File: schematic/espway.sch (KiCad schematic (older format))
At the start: 32 parts, among them J1 CONN_01X02, J2 CONN_01X02, J3 CONN_01X04_MALE, SW1 SW_Push, U1 LM1117-3.3, U2 ESP-12E, U3 DRV8835, U4 LSM6DS3

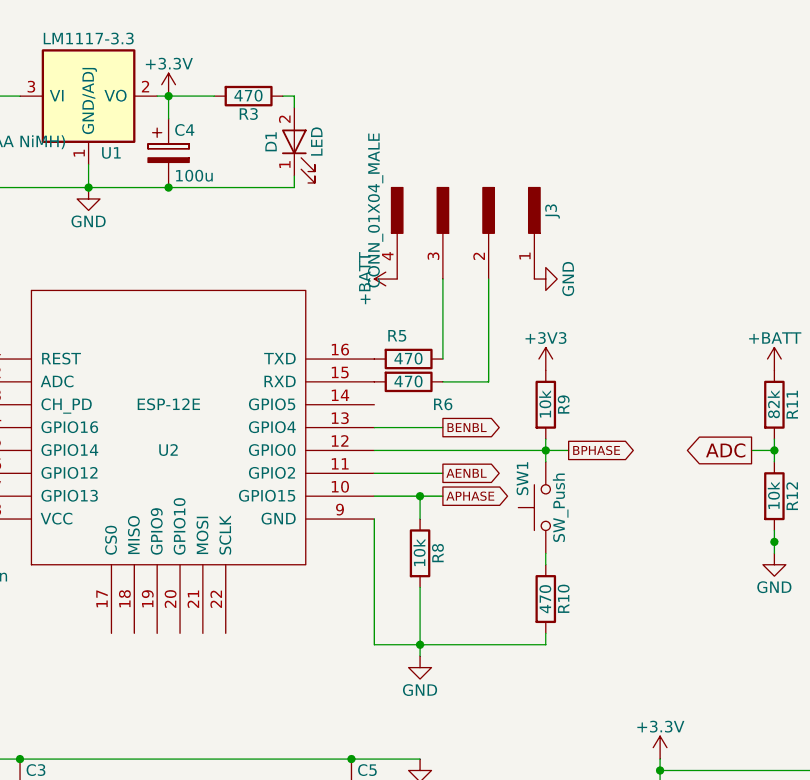
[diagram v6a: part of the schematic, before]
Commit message: Schematic: change resistor values, break out extra GPIO pin
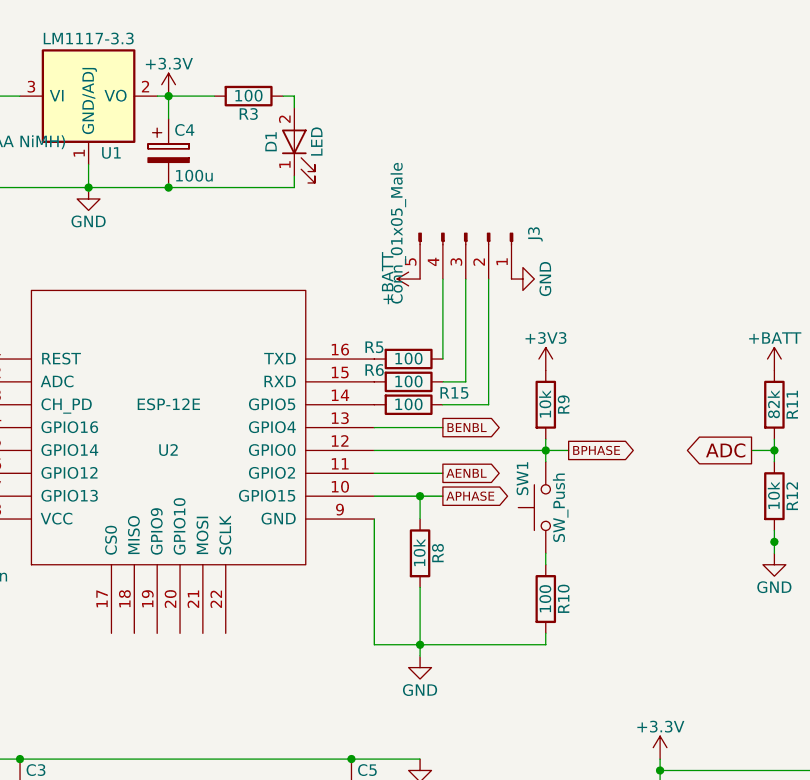
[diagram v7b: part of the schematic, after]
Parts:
- removed J3: CONN_01X04_MALE, Pin_Headers:Pin_Header_Angled_1x04_Pitch2.54mm, symbol CONN_01X04_MALE
- added J3: Conn_01x05_Male, Pin_Headers:Pin_Header_Angled_1x05_Pitch2.54mm, symbol Conn_01x05_Male
- added R15: 100, Resistors_SMD:R_0603, symbol R
- R10, R3, R5, R6: value 470 -> 100
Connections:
- net +BATT: now also J3.5 (Pin_5)
- net GND: now also J3.1 (Pin_1)
- net at U2.14 (GPIO5): now also R15.2
- net at R5.1: now also J3.4 (Pin_4)
- net at R6.1: now also J3.3 (Pin_3)
- new net: J3.2 (Pin_2), R15.1
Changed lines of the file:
@@
 U 1 1 59B6D1FB
 P 7250 2350
-F 0 "R5" V 7150 2300 50  0000 C CNN
-F 1 "470" V 7250 2350 50  0000 C CNN
+F 0 "R5" V 7200 2200 50  0000 C CNN
+F 1 "100" V 7250 2350 50  0000 C CNN
 F 2 "Resistors_SMD:R_0603" V 7180 2350 50  0001 C CNN
 F 3 "" H 7250 2350 50  0001 C CNN
@@
 U 1 1 59B6D22A
 P 7250 2450
-F 0 "R6" V 7350 2600 50  0000 C CNN
-F 1 "470" V 7250 2450 50  0000 C CNN
+F 0 "R6" V 7200 2300 50  0000 C CNN
+F 1 "100" V 7250 2450 50  0000 C CNN
 F 2 "Resistors_SMD:R_0603" V 7180 2450 50  0001 C CNN
 F 3 "" H 7250 2450 50  0001 C CNN
@@
 L GND #PWR05
 U 1 1 59B8139A
-P 7800 2000
-F 0 "#PWR05" H 7800 1750 50  0001 C CNN
-F 1 "GND" H 7800 1850 50  0000 C CNN
-F 2 "" H 7800 2000 50  0001 C CNN
-F 3 "" H 7800 2000 50  0001 C CNN
-	1    7800 2000
+P 7700 2000
+F 0 "#PWR05" H 7700 1750 50  0001 C CNN
+F 1 "GND" H 7700 1850 50  0000 C CNN
+F 2 "" H 7700 2000 50  0001 C CNN
+F 3 "" H 7700 2000 50  0001 C CNN
+	1    7700 2000
 	0    -1   -1   0
 $EndComp
@@
 P 7850 3400
 F 0 "R10" V 7930 3400 50  0000 C CNN
-F 1 "470" V 7850 3400 50  0000 C CNN
+F 1 "100" V 7850 3400 50  0000 C CNN
 F 2 "Resistors_SMD:R_0603" V 7780 3400 50  0001 C CNN
 F 3 "" H 7850 3400 50  0001 C CNN
@@
 $EndComp
 $Comp
-L CONN_01X04_MALE J3
-U 1 1 59B95DFA
-P 7500 1700
-F 0 "J3" H 7500 2075 50  0000 C CNN
-F 1 "CONN_01X04_MALE" H 7500 1300 50  0000 C CNN
-F 2 "Pin_Headers:Pin_Header_Angled_1x04_Pitch2.54mm" H 7500 2000 50  0001 C CNN
-F 3 "" H 7500 2000 50  0001 C CNN
-	1    7500 1700
-	0    1    1    0
-$EndComp
-$Comp
 L DRV8835 U3
 U 1 1 59BA4BA8
@@
 P 6550 1200
 F 0 "R3" V 6630 1200 50  0000 C CNN
-F 1 "470" V 6550 1200 50  0000 C CNN
+F 1 "100" V 6550 1200 50  0000 C CNN
 F 2 "Resistors_SMD:R_0603" V 6480 1200 50  0001 C CNN
 F 3 "" H 6550 1200 50  0001 C CNN
@@
 Connection ~ 7300 3600
 Wire Wire Line
-	7400 2450 7600 2450
-Wire Wire Line
-	7600 2450 7600 2000
-Wire Wire Line
 	7400 2350 7400 2000
 Wire Wire Line
@@
 L +BATT #PWR019
 U 1 1 5A1E0D39
-P 7200 2000
-F 0 "#PWR019" H 7200 1850 50  0001 C CNN
-F 1 "+BATT" H 7200 2140 50  0000 C CNN
-F 2 "" H 7200 2000 50  0001 C CNN
-F 3 "" H 7200 2000 50  0001 C CNN
-	1    7200 2000
+P 7300 2000
+F 0 "#PWR019" H 7300 1850 50  0001 C CNN
+F 1 "+BATT" H 7300 2140 50  0000 C CNN
+F 2 "" H 7300 2000 50  0001 C CNN
+F 3 "" H 7300 2000 50  0001 C CNN
+	1    7300 2000
 	0    -1   -1   0
 $EndComp
+$Comp
+L Conn_01x05_Male J3
+U 1 1 5A42CC5F
+P 7500 1800
+F 0 "J3" H 7500 2100 50  0000 C CNN
+F 1 "Conn_01x05_Male" H 7500 1500 50  0000 C CNN
+F 2 "Pin_Headers:Pin_Header_Angled_1x05_Pitch2.54mm" H 7500 1800 50  0001 C CNN
+F 3 "" H 7500 1800 50  0001 C CNN
+	1    7500 1800
+	0    1    1    0
+$EndComp
+$Comp
+L R R15
+U 1 1 5A42CEC2
+P 7250 2550
+F 0 "R15" V 7200 2750 50  0000 C CNN
+F 1 "100" V 7250 2550 50  0000 C CNN
+F 2 "Resistors_SMD:R_0603" V 7180 2550 50  0001 C CNN
+F 3 "" H 7250 2550 50  0001 C CNN
+	1    7250 2550
+	0    1    1    0
+$EndComp
+Wire Wire Line
+	7400 2450 7500 2450
+Wire Wire Line
+	7500 2450 7500 2000
+Wire Wire Line
+	7400 2550 7600 2550
+Wire Wire Line
+	7600 2550 7600 2000
 $EndSCHEMATC

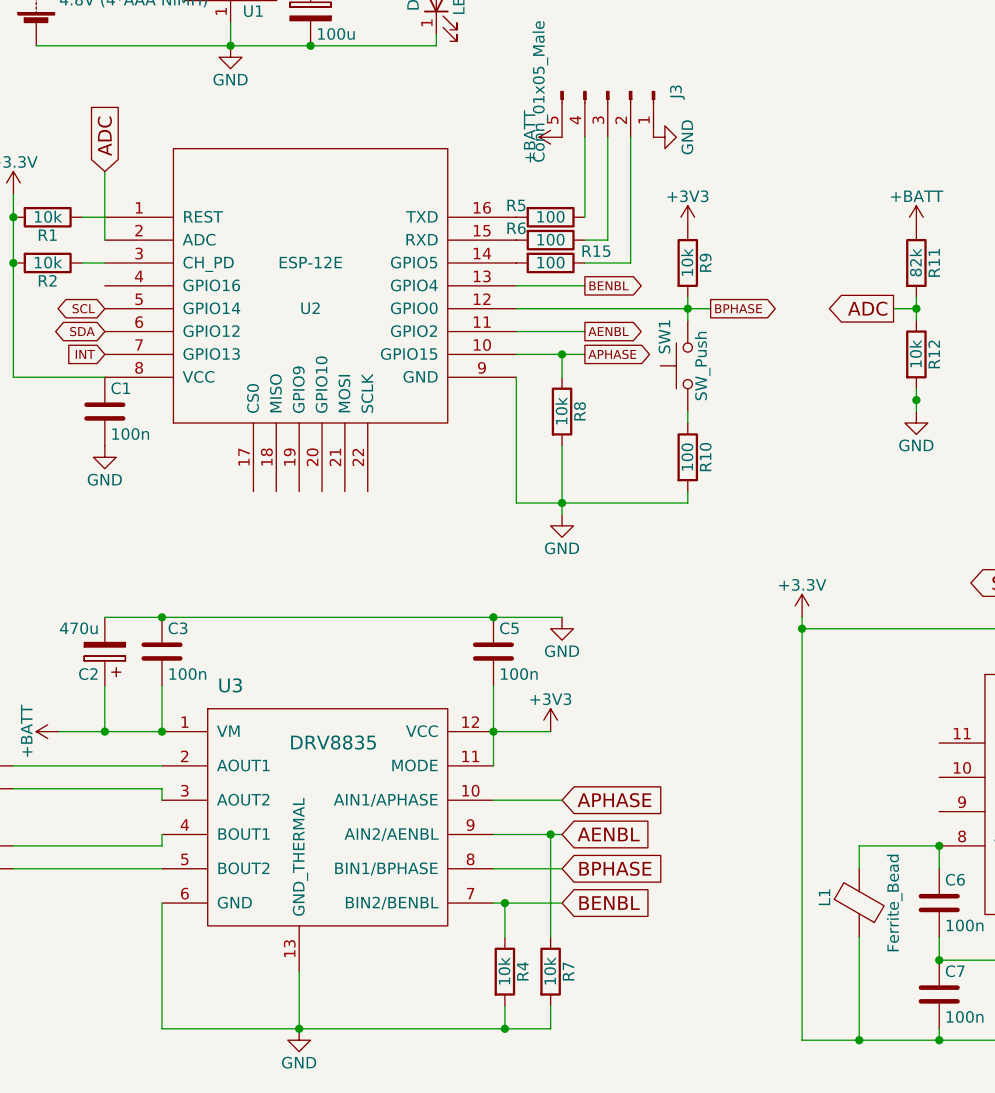
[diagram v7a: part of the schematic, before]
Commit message: schematic & pcb: pullup fixes etc
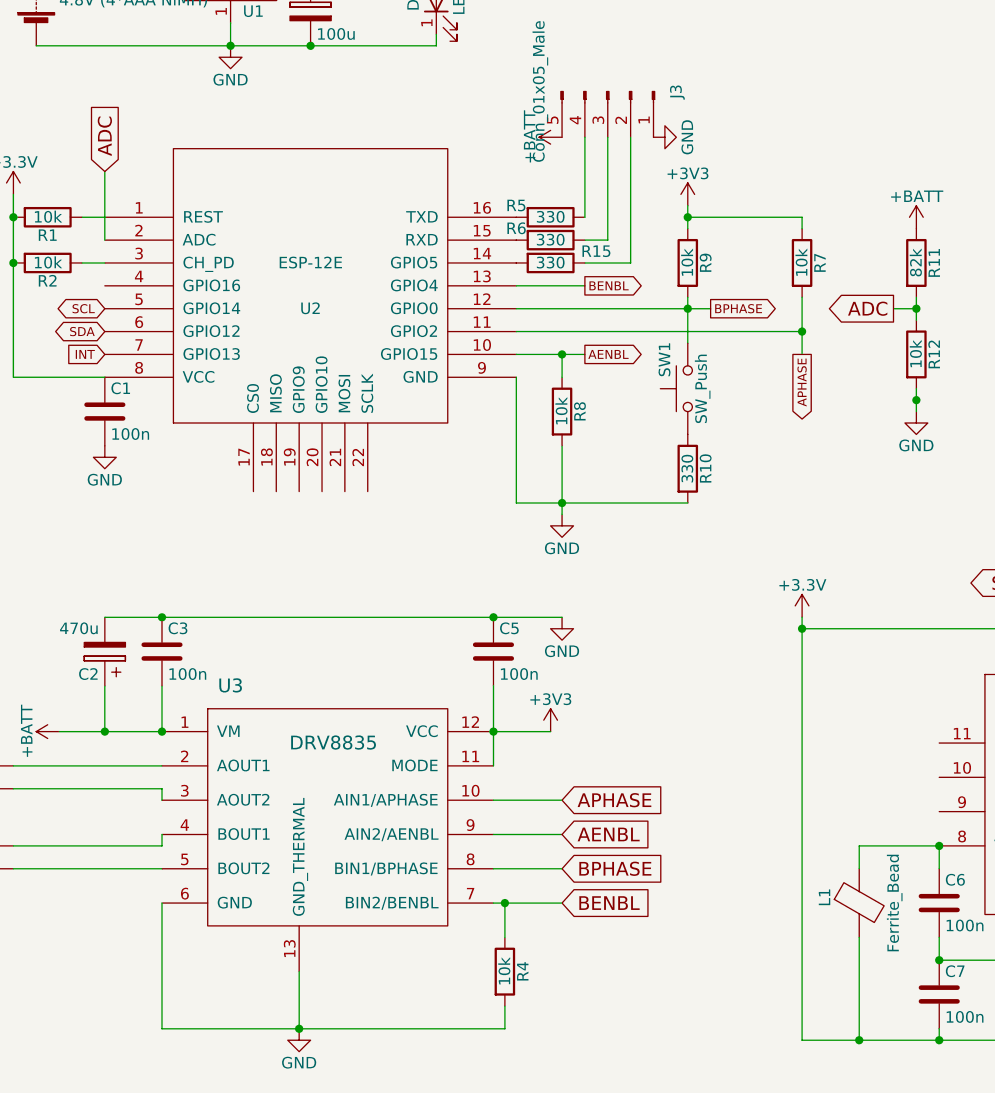
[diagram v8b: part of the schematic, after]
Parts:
- R10, R15, R5, R6: value 100 -> 330
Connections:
- net +3V3: now also R7.1
- net AENBL: now also R8.1, U2.10 (GPIO15); no longer R7.1, U2.11 (GPIO2)
- net APHASE: now also R7.2, U2.11 (GPIO2); no longer R8.1, U2.10 (GPIO15)
- net GND: no longer R7.2
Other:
- moved on the sheet: R10, SW1
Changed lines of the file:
@@
 P 7250 2350
 F 0 "R5" V 7200 2200 50  0000 C CNN
-F 1 "100" V 7250 2350 50  0000 C CNN
+F 1 "330" V 7250 2350 50  0000 C CNN
 F 2 "Resistors_SMD:R_0603" V 7180 2350 50  0001 C CNN
 F 3 "" H 7250 2350 50  0001 C CNN
@@
 P 7250 2450
 F 0 "R6" V 7200 2300 50  0000 C CNN
-F 1 "100" V 7250 2450 50  0000 C CNN
+F 1 "330" V 7250 2450 50  0000 C CNN
 F 2 "Resistors_SMD:R_0603" V 7180 2450 50  0001 C CNN
 F 3 "" H 7250 2450 50  0001 C CNN
@@
 L R R10
 U 1 1 59B81CF0
-P 7850 3400
-F 0 "R10" V 7930 3400 50  0000 C CNN
-F 1 "100" V 7850 3400 50  0000 C CNN
-F 2 "Resistors_SMD:R_0603" V 7780 3400 50  0001 C CNN
-F 3 "" H 7850 3400 50  0001 C CNN
-	1    7850 3400
+P 7850 3450
+F 0 "R10" V 7930 3450 50  0000 C CNN
+F 1 "330" V 7850 3450 50  0000 C CNN
+F 2 "Resistors_SMD:R_0603" V 7780 3450 50  0001 C CNN
+F 3 "" H 7850 3450 50  0001 C CNN
+	1    7850 3450
 	1    0    0    -1
 $EndComp
@@
 L SW_Push SW1
 U 1 1 59B81E53
-P 7850 3000
-F 0 "SW1" H 7900 3100 50  0000 L CNN
-F 1 "SW_Push" H 7850 2940 50  0000 C CNN
-F 2 "Buttons_Switches_SMD:SW_SPST_KMR2" H 7850 3200 50  0001 C CNN
-F 3 "" H 7850 3200 50  0001 C CNN
-	1    7850 3000
+P 7850 3100
+F 0 "SW1" H 7900 3200 50  0000 L CNN
+F 1 "SW_Push" H 7850 3040 50  0000 C CNN
+F 2 "Buttons_Switches_SMD:SW_SPST_KMR2" H 7850 3300 50  0001 C CNN
+F 3 "" H 7850 3300 50  0001 C CNN
+	1    7850 3100
 	0    -1   -1   0
 $EndComp
@@
 BENBL
 Text GLabel 7400 2950 2    39   Output ~ 0
-APHASE
+AENBL
 $Comp
 L Battery BT1
@@
 Connection ~ 6200 1600
 $Comp
-L R R7
-U 1 1 59E13532
-P 7250 5650
-F 0 "R7" V 7330 5650 50  0000 C CNN
-F 1 "10k" V 7250 5650 50  0000 C CNN
-F 2 "Resistors_SMD:R_0603" V 7180 5650 50  0001 C CNN
-F 3 "" H 7250 5650 50  0001 C CNN
-	1    7250 5650
-	1    0    0    -1
-$EndComp
-$Comp
 L GND #PWR015
 U 1 1 5A19A5EC
@@
 Wire Wire Line
 	5550 5350 5550 5900
-Wire Wire Line
-	5550 5900 7250 5900
 Connection ~ 6150 5900
 Wire Wire Line
@@
 Wire Wire Line
 	7050 5900 7050 5800
-Connection ~ 7050 5900
 Wire Wire Line
 	7100 2950 7400 2950
@@
 Wire Wire Line
 	7100 3050 7100 3600
-Text GLabel 7400 2850 2    39   Output ~ 0
-AENBL
-Wire Wire Line
-	7400 2850 7100 2850
+Text GLabel 8350 2950 3    39   Output ~ 0
+APHASE
+Wire Wire Line
+	7100 2850 8350 2850
 Text GLabel 7400 2650 2    39   Output ~ 0
 BENBL
@@
 	7000 5050 7300 5050
 Wire Wire Line
-	7250 5050 7250 5500
-Connection ~ 7250 5050
-Wire Wire Line
-	7250 5900 7250 5800
-Wire Wire Line
 	7300 5200 7000 5200
 Wire Wire Line
@@
 Wire Wire Line
 	10200 4650 10050 4650
-Wire Wire Line
-	7850 3600 7850 3550
 Connection ~ 8850 3150
-Wire Wire Line
-	7850 3250 7850 3200
 $Comp
 L R R9
@@
 L +3V3 #PWR018
 U 1 1 5A1DE58F
-P 7850 2400
-F 0 "#PWR018" H 7850 2250 50  0001 C CNN
-F 1 "+3V3" H 7850 2540 50  0000 C CNN
-F 2 "" H 7850 2400 50  0001 C CNN
-F 3 "" H 7850 2400 50  0001 C CNN
-	1    7850 2400
-	1    0    0    -1
-$EndComp
-Wire Wire Line
-	7850 2700 7850 2800
+P 7850 2300
+F 0 "#PWR018" H 7850 2150 50  0001 C CNN
+F 1 "+3V3" H 7850 2440 50  0000 C CNN
+F 2 "" H 7850 2300 50  0001 C CNN
+F 3 "" H 7850 2300 50  0001 C CNN
+	1    7850 2300
+	1    0    0    -1
+$EndComp
+Wire Wire Line
+	7850 2700 7850 2900
 Text GLabel 7950 2750 2    39   Output ~ 0
 BPHASE
@@
 P 7250 2550
 F 0 "R15" V 7200 2750 50  0000 C CNN
-F 1 "100" V 7250 2550 50  0000 C CNN
+F 1 "330" V 7250 2550 50  0000 C CNN
 F 2 "Resistors_SMD:R_0603" V 7180 2550 50  0001 C CNN
 F 3 "" H 7250 2550 50  0001 C CNN
@@
 Wire Wire Line
 	7600 2550 7600 2000
+Wire Wire Line
+	5550 5900 7050 5900
+Wire Wire Line
+	7850 2300 7850 2400
+$Comp
+L R R7
+U 1 1 5A442EE2
+P 8350 2550
+F 0 "R7" V 8430 2550 50  0000 C CNN
+F 1 "10k" V 8350 2550 50  0000 C CNN
+F 2 "Resistors_SMD:R_0603" V 8280 2550 50  0001 C CNN
+F 3 "" H 8350 2550 50  0001 C CNN
+	1    8350 2550
+	1    0    0    -1
+$EndComp
+Wire Wire Line
+	8350 2700 8350 2950
+Wire Wire Line
+	8350 2400 8350 2350
+Wire Wire Line
+	8350 2350 7850 2350
+Connection ~ 7850 2350
+Connection ~ 8350 2850
 $EndSCHEMATC
